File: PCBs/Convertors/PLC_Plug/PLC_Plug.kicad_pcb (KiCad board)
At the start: 2 copper layers, 23 parts, among them J1 RO21, J10 AOV2.3, J11 AOV2.4, J12 RS485-2.1, J13 RS485-2.1, J14 AO, J15 AO, J16 DO, J17 DI, J18 DI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

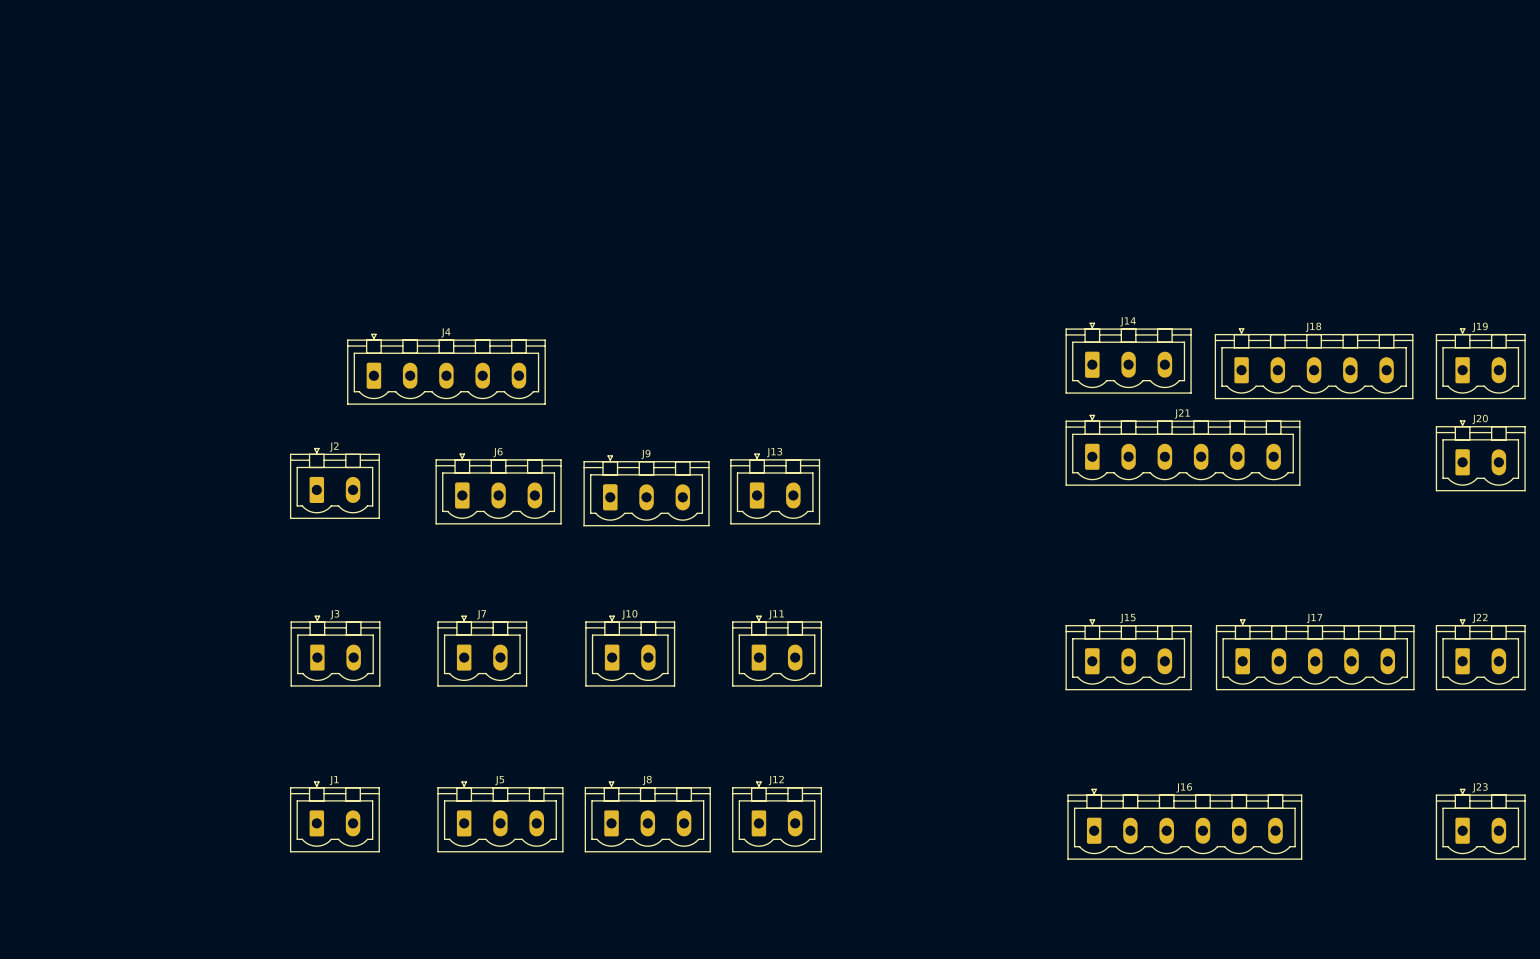
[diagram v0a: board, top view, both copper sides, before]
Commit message: Update PLC adapter
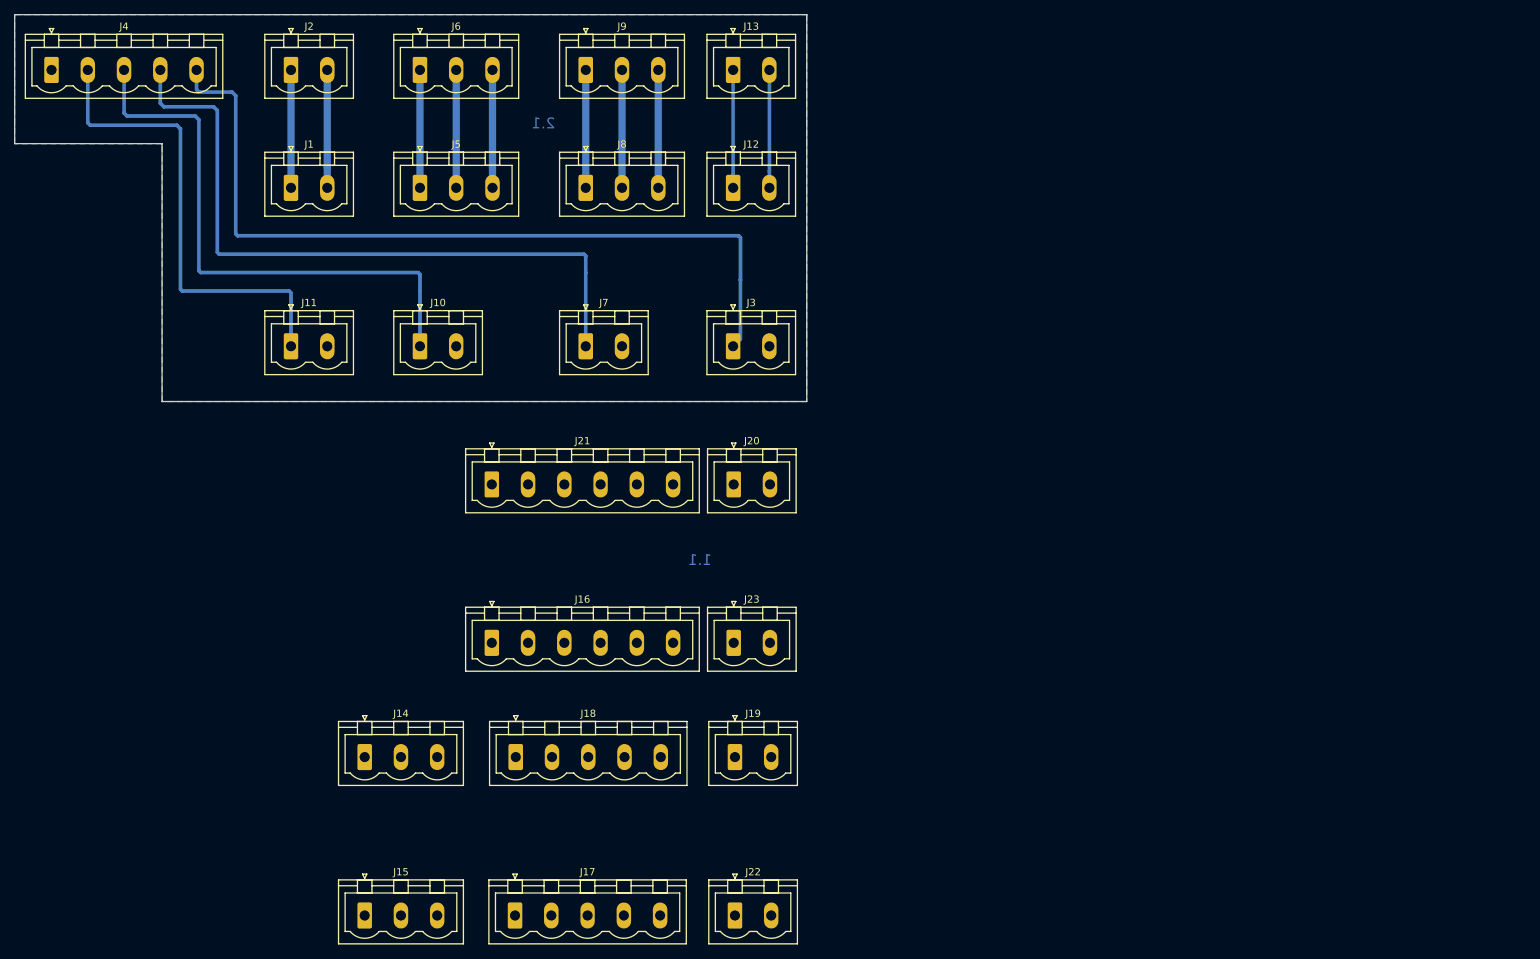
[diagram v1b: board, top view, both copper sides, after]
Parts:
- moved J14 114.0 mm to (74.7, 122.7)
- moved J19 113.6 mm to (125.7, 122.7)
- moved J18 113.4 mm to (95.5, 122.7)
- moved J17 106.3 mm to (95.4, 144.5)
- moved J15 106.3 mm to (74.7, 144.5)
- moved J22 106.3 mm to (125.7, 144.5)
- moved J23 103.8 mm to (125.6, 106.9)
- moved J20 100.6 mm to (125.6, 85.1)
- moved J5 87.8 mm to (82.3, 44.2)
- moved J1 87.7 mm to (64.5, 44.2)
- moved J12 87.7 mm to (125.5, 44.2)
- moved J8 87.7 mm to (105.2, 44.2)
- moved J16 87.0 mm to (92.2, 106.9)
- moved J21 82.9 mm to (92.2, 85.1)
- moved J11 77.5 mm to (64.5, 66.0)
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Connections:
- J1 pad 1: /COM21 -> /RO2.1
- J1 pad 2: /RO2.1 -> /COM21
- J10 pad 1: /GND-A -> /AOV2.3
- J10 pad 2: /AOV2.3 -> /GND-A
- J11 pad 1: /GND-A -> /AOV2.4
- J11 pad 2: /AOV2.4 -> /GND-A
- J12 pad 1: /RS485-2.1-A -> /RS485-2.1-B
- J12 pad 2: /RS485-2.1-B -> /RS485-2.1-A
- J13 pad 1: /RS485-2.1-A -> /RS485-2.1-B
- J13 pad 2: /RS485-2.1-B -> /RS485-2.1-A
- J2 pad 1: /COM21 -> /RO2.1
- J2 pad 2: /RO2.1 -> /COM21
- J3 pad 1: /GND-A -> /AOV2.1
- J3 pad 2: /AOV2.1 -> /GND-A
- J4 pad 2: /AOV2.1 -> /AOV2.4
- J4 pad 3: /AOV2.2 -> /AOV2.3
- J4 pad 4: /AOV2.3 -> /AOV2.2
- J4 pad 5: /AOV2.4 -> /AOV2.1
- J5 pad 1: /RO2.3 -> /RO2.2
- J5 pad 3: /RO2.2 -> /RO2.3
- J6 pad 1: /RO2.3 -> /RO2.2
- J6 pad 3: /RO2.2 -> /RO2.3
- J7 pad 1: /GND-A -> /AOV2.2
- J7 pad 2: /AOV2.2 -> /GND-A
- J8 pad 1: /RO2.5 -> /RO2.4
- J8 pad 3: /RO2.4 -> /RO2.5
- J9 pad 1: /RO2.5 -> /RO2.4
- J9 pad 3: /RO2.4 -> /RO2.5
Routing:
- net /AOV2.1: track 0.00 -> 112.8 mm
- net /AOV2.2: track 0.00 -> 95.9 mm
- net /AOV2.3: track 0.00 -> 78.1 mm
- net /AOV2.4: track 0.00 -> 65.3 mm
- net /RS485-2.1-B: track 0.00 -> 18.0 mm
- net /RS485-2.1-A: track 0.00 -> 16.3 mm
- net /RO2.5: track 0.00 -> 16.3 mm
- net /RO2.4: track 0.00 -> 16.3 mm
- net /RO2.3: track 0.00 -> 16.3 mm
- net /RO2.2: track 0.00 -> 16.3 mm
- net /RO2.1: track 0.00 -> 16.3 mm
- net /COM245: track 0.00 -> 16.3 mm
- net /COM223: track 0.00 -> 16.3 mm
- net /COM21: track 0.00 -> 16.3 mm
- added copper zone on B.Cu, net /GND-A
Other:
- board outline added: 109.2 x 53.3 mm
- net class Analog Lines added: clearance 0.2, trace_width 0.5, via_dia 0.8, via_drill 0.4
- net class Power added: clearance 0.2, trace_width 2, via_dia 0.8, via_drill 0.4
- net class Relay Lines added: clearance 0.2, trace_width 1, via_dia 0.8, via_drill 0.4
- board text added: "1.1"
- board text added: "2.1"
